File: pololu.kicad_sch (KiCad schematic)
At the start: 11 parts, among them J15 pololu, J16 pololu, J17 pololu, J18 pololu, J19 pololu, J20 pololu

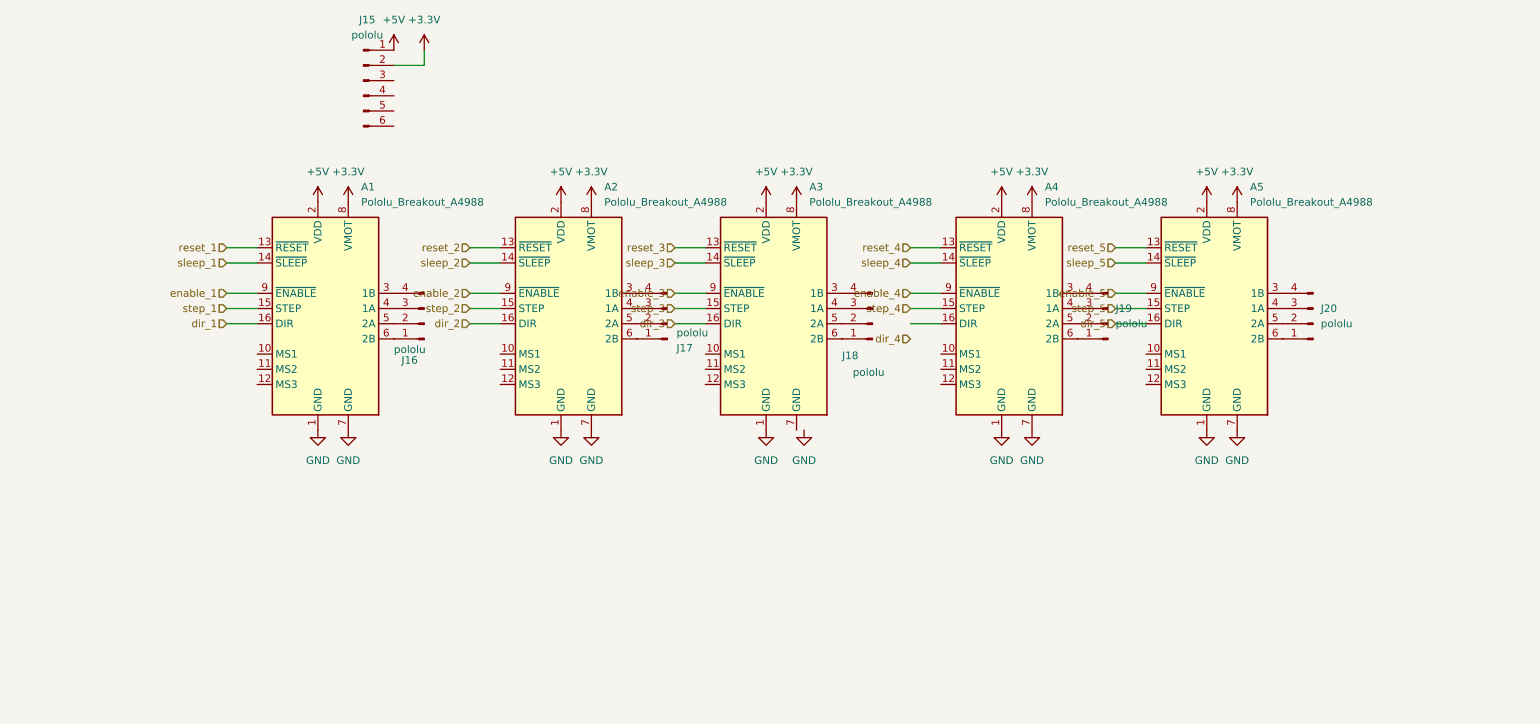
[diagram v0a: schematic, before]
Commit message: feat: integrate zigbee sheet + R 0603→0805 footprint update
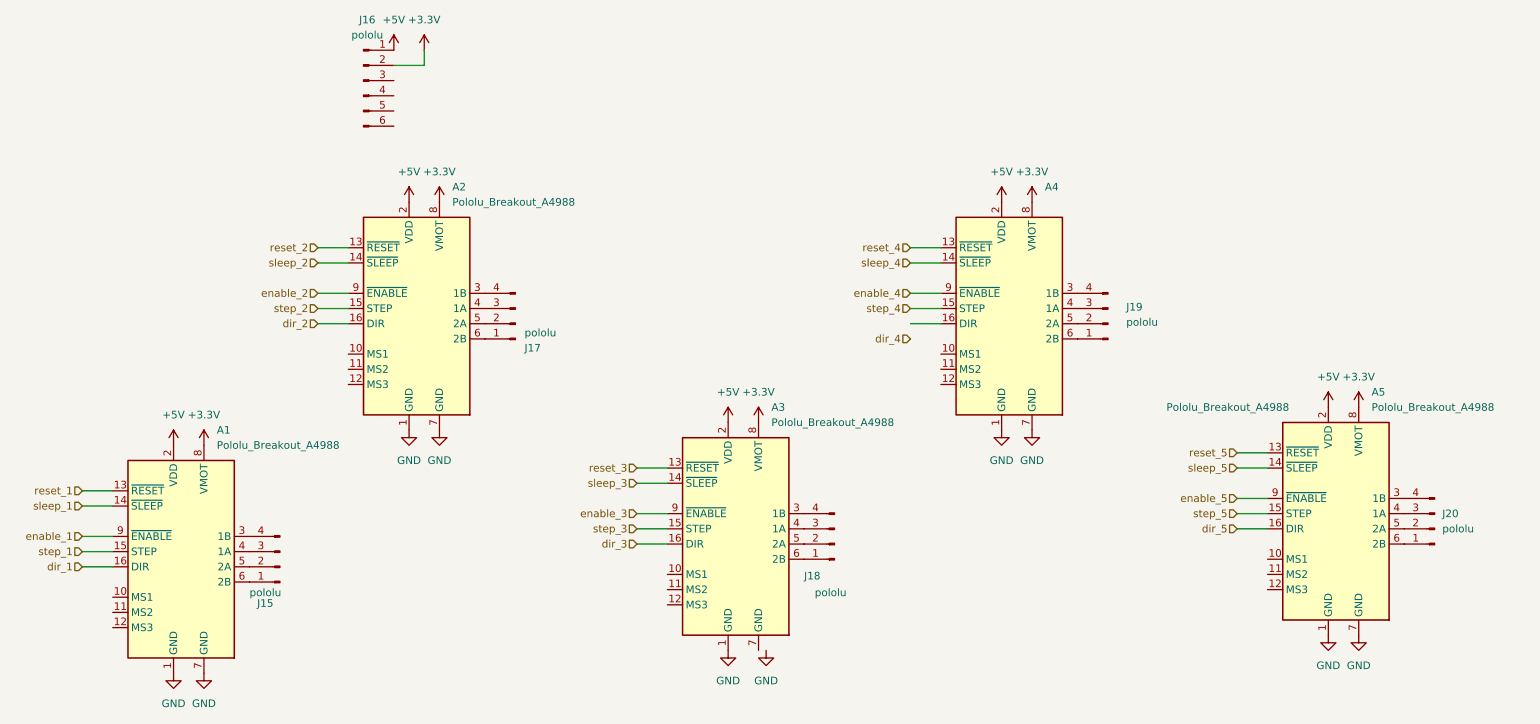
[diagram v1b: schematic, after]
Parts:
- renumbered J16 to J15, J15 to J16
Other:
- moved on the sheet: A1, A2, A3, A5, J15, J17, J18, J20

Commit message: feat: add MA240011 module sheet with labeled pins + Altium socket footprint
Esquemático
- Nueva hoja hija MA240011.kicad_sch (módulo PIC32 TQFP-100) referenciada
  desde la hoja MA240011 de mcu.kicad_sch
- mcu.kicad_sch: los 83 pines jerárquicos de MA240011 quedan rotulados con un
  label local del mismo nombre; 81 de ellos con un tramo de wire de 2.54 mm
  (un label solo no conecta a un pin de hoja) y RD4/RD5 sobre el wire existente
- mcu.kicad_sch: borde derecho del sheet 104.775 -> 106.68 mm y sus 41 pines,
  para quedar en grilla de 1.27 mm (evita 41 avisos endpoint_off_grid)
- ERC: 341 -> 158 violaciones; pin_not_connected 120 -> 39,
  isolated_pin_label 113 -> 10, endpoint_off_grid 6 -> 6
- power / zigbee / oled / pololu / cnc_pic32: pines MS1-MS3, conectores y
  anotacion de netnames

PCB
- Referencia de los 132 footprints a size 0.8 x 0.8 mm y thickness 0.12 mm
  (render_cache obsoleto eliminado para forzar el re-render)

Footprints
- lib/altium.pretty/MA240011_Socket_TQFP100_100pin.kicad_mod: zocalo adaptador
  de 100 pines TH pitch 1.27 mm convertido desde altium/Multimedia/MM20141127.PcbDoc
  (J4, patron MA240011); pads girados 90 grados sentido horario
- fp-lib-table: alta de la biblioteca "altium" (${KIPRJMOD}/lib/altium.pretty)

.gitignore
- Ignorar altium/, tmp/ y *.bkp (backups de KiCad)
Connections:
- net dir_4: now also A4.16 (DIR)
- net MS1: now reaches A3.10 (MS1)
- net MS1: now also A1.10 (MS1), A2.10 (MS1), A4.10 (MS1), A5.10 (MS1)
- net MS2: now reaches A3.11 (MS2)
- net MS2: now also A1.11 (MS2), A2.11 (MS2), A4.11 (MS2), A5.11 (MS2)
- net MS3: now reaches A3.12 (MS3)
- net MS3: now also A1.12 (MS3), A2.12 (MS3), A4.12 (MS3), A5.12 (MS3)
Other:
- moved on the sheet: J15, J17, J18, J19, J20

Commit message: add files
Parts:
- added JP10, JP13, JP16, JP19, JP22: MS2, Jumper:SolderJumper-2_P1.3mm_Open_RoundedPad1.0x1.5mm, symbol Jumper:Jumper_2_Bridged
- added JP11, JP14, JP17, JP20, JP23: MS3, Jumper:SolderJumper-2_P1.3mm_Open_RoundedPad1.0x1.5mm, symbol Jumper:Jumper_2_Bridged
- added JP12, JP15, JP18, JP21, JP9: MS1, Jumper:SolderJumper-2_P1.3mm_Open_RoundedPad1.0x1.5mm, symbol Jumper:Jumper_2_Bridged
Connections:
- net GND: now also A3.7 (GND)
- net MS1: now also JP12.1 (A), JP15.1 (A), JP18.1 (A), JP21.1 (A), JP9.1 (A); no longer A1.10 (MS1), A2.10 (MS1), A3.10 (MS1), A4.10 (MS1), A5.10 (MS1)
- net MS2: now also JP10.1 (A), JP13.1 (A), JP16.1 (A), JP19.1 (A), JP22.1 (A); no longer A1.11 (MS2), A2.11 (MS2), A3.11 (MS2), A4.11 (MS2), A5.11 (MS2)
- net MS3: now also JP11.1 (A), JP14.1 (A), JP17.1 (A), JP20.1 (A), JP23.1 (A); no longer A1.12 (MS3), A2.12 (MS3), A3.12 (MS3), A4.12 (MS3), A5.12 (MS3)
- new net: A3.10 (MS1), JP12.2 (B)
- new net: A3.11 (MS2), JP13.2 (B)
- new net: A3.12 (MS3), JP14.2 (B)
- new net: A5.10 (MS1), JP21.2 (B)
- new net: A5.11 (MS2), JP22.2 (B)
- new net: A5.12 (MS3), JP23.2 (B)
- new net: A1.10 (MS1), JP9.2 (B)
- new net: A1.12 (MS3), JP11.2 (B)
- new net: A2.11 (MS2), JP16.2 (B)
- new net: A4.10 (MS1), JP18.2 (B)
- new net: A4.11 (MS2), JP19.2 (B)
- new net: A4.12 (MS3), JP20.2 (B)
- new net: A1.11 (MS2), JP10.2 (B)
- new net: A2.10 (MS1), JP15.2 (B)
- new net: A2.12 (MS3), JP17.2 (B)
- no-connect marks 0 -> 4

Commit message: updated
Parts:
- added A10, A6, A7, A8, A9: Pololu_Breakout_DRV8825, kiC:HTSSOP-28-EP_IC_TPS61196PWPRQ1, symbol Driver_Motor:Pololu_Breakout_DRV8825
- added JP25, JP26, JP27, JP28, JP29, JP30, JP31, JP32, JP33, JP34, JP35, JP36, JP37, JP38, JP39, JP40, JP41, JP42, JP43, JP44: MS3, Jumper:SolderJumper-2_P1.3mm_Open_RoundedPad1.0x1.5mm, symbol Jumper:Jumper_2_Bridged
- A1, A2, A3, A4, A5, J15, J16, J17, J18, J19, J20, JP10, JP11, JP12, JP13, JP14, JP15, JP16, JP17, JP18, JP19, JP20, JP21, JP22, JP23, JP9: now left out of the parts list
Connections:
- net reset_2 is gone; now on net reset: A2.13 (~{RESET})
- net reset_3 is gone; now on net reset: A3.13 (~{RESET})
- net reset_4 is gone; now on net reset: A4.13 (~{RESET})
- net reset_5 is gone; now on net reset: A5.13 (~{RESET})
- net sleep_2 is gone; now on net sleep: A2.14 (~{SLEEP})
- net sleep_3 is gone; now on net sleep: A3.14 (~{SLEEP})
- net sleep_4 is gone; now on net sleep: A4.14 (~{SLEEP})
- net sleep_5 is gone; now on net sleep: A5.14 (~{SLEEP})
- net +3.3V: now also A1.2 (VDD), A2.2 (VDD), A3.2 (VDD), A4.2 (VDD), A5.2 (VDD); no longer A1.8 (VMOT), A2.8 (VMOT), A3.8 (VMOT), A4.8 (VMOT), A5.8 (VMOT), J16.2 (Pin_2)
- net GND: now also A10.1 (GND), A10.7 (GND), A6.1 (GND), A6.7 (GND), A7.1 (GND), A7.7 (GND), A8.1 (GND), A8.7 (GND), A9.1 (GND), A9.7 (GND)
- net MS1: now also J16.3 (Pin_3)
- net MS2: now also J16.4 (Pin_4)
- net MS3: now also J16.5 (Pin_5)
- net dir_1: now also A7.16 (DIR)
- net dir_2: now also A6.16 (DIR)
- net dir_3: now also A8.16 (DIR)
- net dir_4: now also A10.16 (DIR)
- net dir_5: now also A9.16 (DIR)
- net enable_1: now also A7.9 (~{EN})
- net enable_2: now also A6.9 (~{EN})
- net enable_3: now also A8.9 (~{EN})
- net enable_4: now also A10.9 (~{EN})
- net enable_5: now also A9.9 (~{EN})
- net step_1: now also A7.15 (STEP)
- net step_2: now also A6.15 (STEP)
- net step_3: now also A8.15 (STEP)
- net step_4: now also A10.15 (STEP)
- net step_5: now also A9.15 (STEP)
- net 2B_5: now reaches A5.6 (2B), J20.1 (Pin_1)
- net 2B_5: now also JP40.2 (B)
- net 2A_5: now reaches A5.5 (2A), J20.2 (Pin_2)
- net 2A_5: now also JP39.2 (B)
- net 1A_5: now reaches A5.4 (1A), J20.3 (Pin_3)
- net 1A_5: now also JP38.2 (B)
- net 1B_5: now reaches A5.3 (1B), J20.4 (Pin_4)
- net 1B_5: now also JP37.2 (B)
- net MS1_DRV8825_3: now reaches A3.10 (MS1), JP12.2 (B)
- net MS1_DRV8825_3: now also A8.10 (M0)
- net MS2_DRV8825_3: now reaches A3.11 (MS2), JP13.2 (B)
- net MS2_DRV8825_3: now also A8.11 (M1)
- net MS3_DRV8825_3: now reaches A3.12 (MS3), JP14.2 (B)
- net MS3_DRV8825_3: now also A8.12 (M2)
- net 1B_3: now reaches A3.3 (1B), J18.4 (Pin_4)
- net 1B_3: now also JP41.2 (B)
- net 1A_3: now reaches A3.4 (1A), J18.3 (Pin_3)
- net 1A_3: now also JP42.2 (B)
- net 2A_3: now reaches A3.5 (2A), J18.2 (Pin_2)
- net 2A_3: now also JP43.2 (B)
- net 2B_3: now reaches A3.6 (2B), J18.1 (Pin_1)
- net 2B_3: now also JP44.2 (B)
- net MS1_DRV8825_5: now reaches A5.10 (MS1), JP21.2 (B)
- net MS1_DRV8825_5: now also A9.10 (M0)
- net MS2_DRV8825_5: now reaches A5.11 (MS2), JP22.2 (B)
- net MS2_DRV8825_5: now also A9.11 (M1)
- net MS3_DRV8825_5: now reaches A5.12 (MS3), JP23.2 (B)
- net MS3_DRV8825_5: now also A9.12 (M2)
- net MS1_DRV8825_1: now reaches A1.10 (MS1), JP9.2 (B)
- net MS1_DRV8825_1: now also A7.10 (M0)
- net 2B_1: now reaches A1.6 (2B), J15.1 (Pin_1)
- net 2B_1: now also JP28.2 (B)
- net 2A_1: now reaches A1.5 (2A), J15.2 (Pin_2)
- net 2A_1: now also JP27.2 (B)
- net 1A_1: now reaches A1.4 (1A), J15.3 (Pin_3)
- net 1A_1: now also JP26.2 (B)
- net 1B_1: now reaches A1.3 (1B), J15.4 (Pin_4)
- net 1B_1: now also JP25.2 (B)
- net MS3_DRV8825_1: now reaches A1.12 (MS3), JP11.2 (B)
- net MS3_DRV8825_1: now also A7.12 (M2)
- net MS2_DRV8825_2: now reaches A2.11 (MS2), JP16.2 (B)
- net MS2_DRV8825_2: now also A6.11 (M1)
- net MS1_DRV8825_4: now reaches A4.10 (MS1), JP18.2 (B)
- net MS1_DRV8825_4: now also A10.10 (M0)
- net MS2_DRV8825_4: now reaches A4.11 (MS2), JP19.2 (B)
- net MS2_DRV8825_4: now also A10.11 (M1)
- net MS3_DRV8825_4: now reaches A4.12 (MS3), JP20.2 (B)
- net MS3_DRV8825_4: now also A10.12 (M2)
- net 1B_4: now reaches A4.3 (1B), J19.4 (Pin_4)
- net 1B_4: now also JP33.2 (B)
- net 1A_4: now reaches A4.4 (1A), J19.3 (Pin_3)
- net 1A_4: now also JP34.2 (B)
- net 2A_4: now reaches A4.5 (2A), J19.2 (Pin_2)
- net 2A_4: now also JP35.2 (B)
- net 2B_4: now reaches A4.6 (2B), J19.1 (Pin_1)
- net 2B_4: now also JP36.2 (B)
- net MS2_DRV8825_1: now reaches A1.11 (MS2), JP10.2 (B)
- net MS2_DRV8825_1: now also A7.11 (M1)
- net MS1_DRV8825_2: now reaches A2.10 (MS1), JP15.2 (B)
- net MS1_DRV8825_2: now also A6.10 (M0)
- net MS3_DRV8825_2: now reaches A2.12 (MS3), JP17.2 (B)
- net MS3_DRV8825_2: now also A6.12 (M2)
- net 1B_2: now reaches A2.3 (1B), J17.4 (Pin_4)
- net 1B_2: now also JP29.2 (B)
- net 1A_2: now reaches A2.4 (1A), J17.3 (Pin_3)
- net 1A_2: now also JP30.2 (B)
- net 2A_2: now reaches A2.5 (2A), J17.2 (Pin_2)
- net 2A_2: now also JP31.2 (B)
- net 2B_2: now reaches A2.6 (2B), J17.1 (Pin_1)
- net 2B_2: now also JP32.2 (B)
- removed net +5V: A1.2 (VDD), A2.2 (VDD), A3.2 (VDD), A4.2 (VDD), A5.2 (VDD), J16.1 (Pin_1)
- net reset_1 renamed reset
- net reset: now also A10.13 (~{RST}), A6.13 (~{RST}), A7.13 (~{RST}), A8.13 (~{RST}), A9.13 (~{RST})
- net sleep_1 renamed sleep
- net sleep: now also A10.14 (~{SLP}), A6.14 (~{SLP}), A7.14 (~{SLP}), A8.14 (~{SLP}), A9.14 (~{SLP})
- new net: A6.5 (B1), JP31.1 (A)
- new net: A8.4 (A1), JP41.1 (A)
- new net: A6.4 (A1), JP29.1 (A)
- new net: A10.3 (A2), JP34.1 (A)
- new net: A6.6 (B2), JP32.1 (A)
- new net: A10.4 (A1), JP33.1 (A)
- new net: A10.5 (B1), JP35.1 (A)
- new net: A9.3 (A2), JP38.1 (A)
- new net: A9.4 (A1), JP37.1 (A)
- new net: A9.5 (B1), JP39.1 (A)
- new net: A9.6 (B2), JP40.1 (A)
- new net: A7.6 (B2), JP28.1 (A)
- new net: A7.3 (A2), JP26.1 (A)
- new net: A7.4 (A1), JP25.1 (A)
- new net: A7.5 (B1), JP27.1 (A)
- new net: A6.3 (A2), JP30.1 (A)
- new net: A8.6 (B2), JP44.1 (A)
- new net: A10.6 (B2), JP36.1 (A)
- new net: A8.3 (A2), JP42.1 (A)
- new net: A8.5 (B1), JP43.1 (A)
- new net FLT_1: A7.2 (~{FLT})
- new net FLT_2: A6.2 (~{FLT})
- new net FLT_3: A8.2 (~{FLT})
- new net FLT_4: A10.2 (~{FLT})
- new net FLT_5: A9.2 (~{FLT})
- new net VCC: A1.8 (VMOT), A10.8 (VMOT), A2.8 (VMOT), A3.8 (VMOT), A4.8 (VMOT), A5.8 (VMOT), A6.8 (VMOT), A7.8 (VMOT), A8.8 (VMOT), A9.8 (VMOT), J16.1 (Pin_1)
- new net VDD: J16.2 (Pin_2)
- no-connect marks 4 -> 1
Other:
- moved on the sheet: A1, A2, A3, A4, A5, J15, J16, J17, J18, J19, J20, JP10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
